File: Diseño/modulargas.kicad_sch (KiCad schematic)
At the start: 52 parts, among them J1 MiSD, J10 DLUZ, J11 DISPLAY, J13 RJ45_Shielded, J2 GPS, J3 DS3231, J4 ITG, J5 TECLADO, J7 IMPRESORA, J8 PONTENCIA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

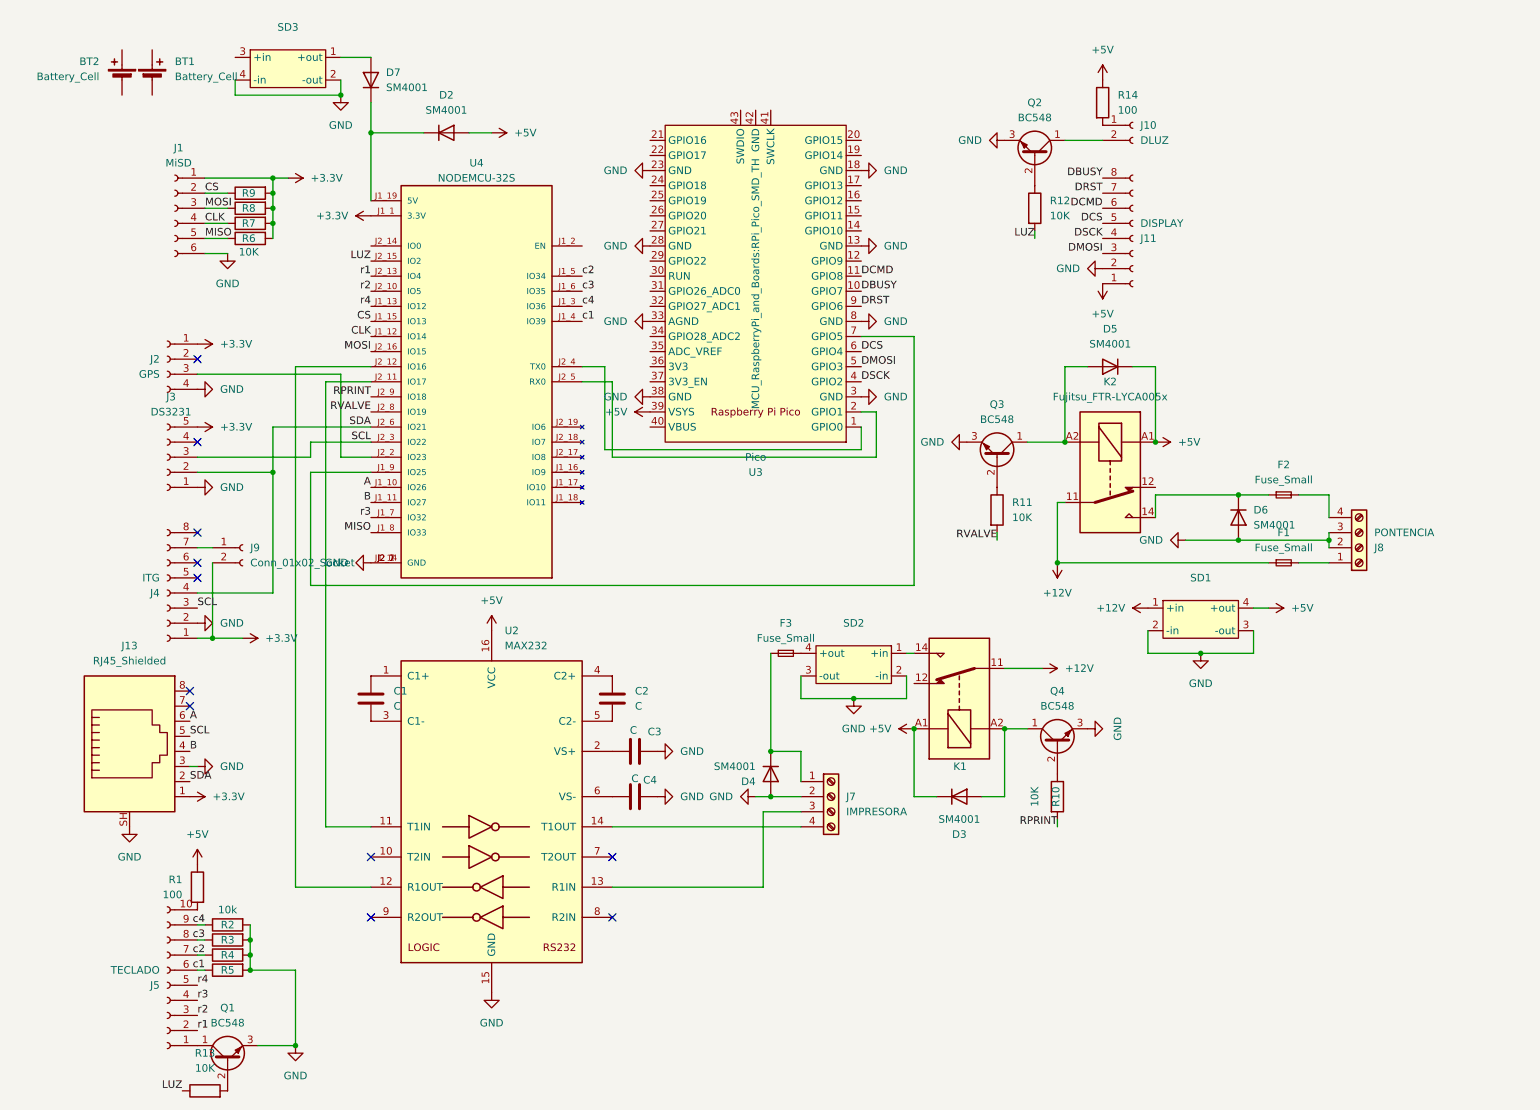
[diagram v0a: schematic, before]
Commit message: Arreglo de errores en el dieseño
Se arreglo la conexion de I2C entre el esp32 y la pico
Se arrglo la conexion del RTC
Se conecto lael cargador a los 5v
Se agrego la conexion para los 5v
Se agrego el punte para las luces del display
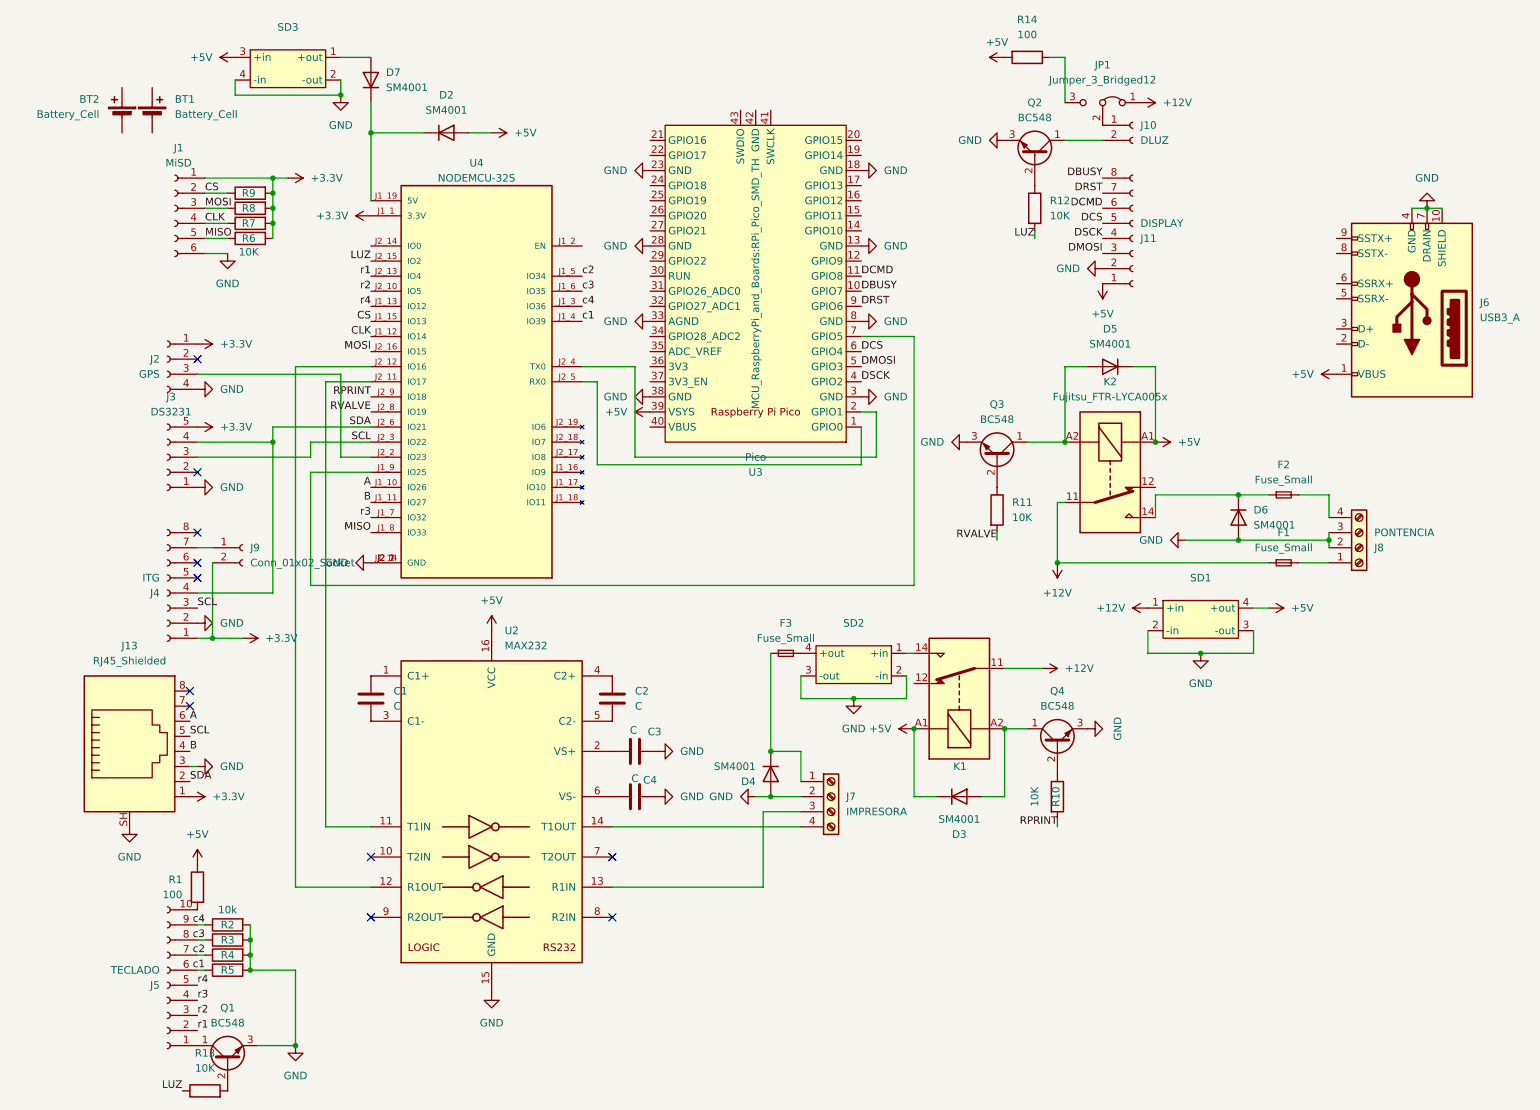
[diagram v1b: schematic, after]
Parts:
- added J6: USB3_A, Connector_USB:USB3_A_Receptacle_Wuerth_692122030100, symbol Connector:USB3_A
- added JP1: Jumper_3_Bridged12, symbol Jumper:Jumper_3_Bridged12
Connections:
- net +12V: now also JP1.1 (A)
- net +5V: now also R14.2, SD3.3 (+in), J6.1 (VBUS); no longer R14.1
- net GND: now also J6.10 (SHIELD), J6.4 (GND), J6.7 (DRAIN)
- net SDA: now also J3.4 (Pin_4); no longer J3.2 (Pin_2)
- net at U3.1 (GPIO0): now also U4.J2_5 (RX0); no longer U4.J2_4 (TX0)
- net at U3.2 (GPIO1): now also U4.J2_4 (TX0); no longer U4.J2_5 (RX0)
- net at J10.1 (Pin_1): now also JP1.2 (C); no longer R14.2
- new net: JP1.3 (B), R14.1
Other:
- moved on the sheet: BT1, BT2, R14
